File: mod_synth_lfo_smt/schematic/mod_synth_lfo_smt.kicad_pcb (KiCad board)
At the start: 2 copper layers, 39.4 x 109.2 mm, 75 parts, among them J1 CV, J2 Conn_02x08_Odd_Even, J3 SIN, J4 COS, J5 TRI, J6 SQR, J7 RAMP UP, J8 RAMP DOWN, Q1 BC550, Q2 BC550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

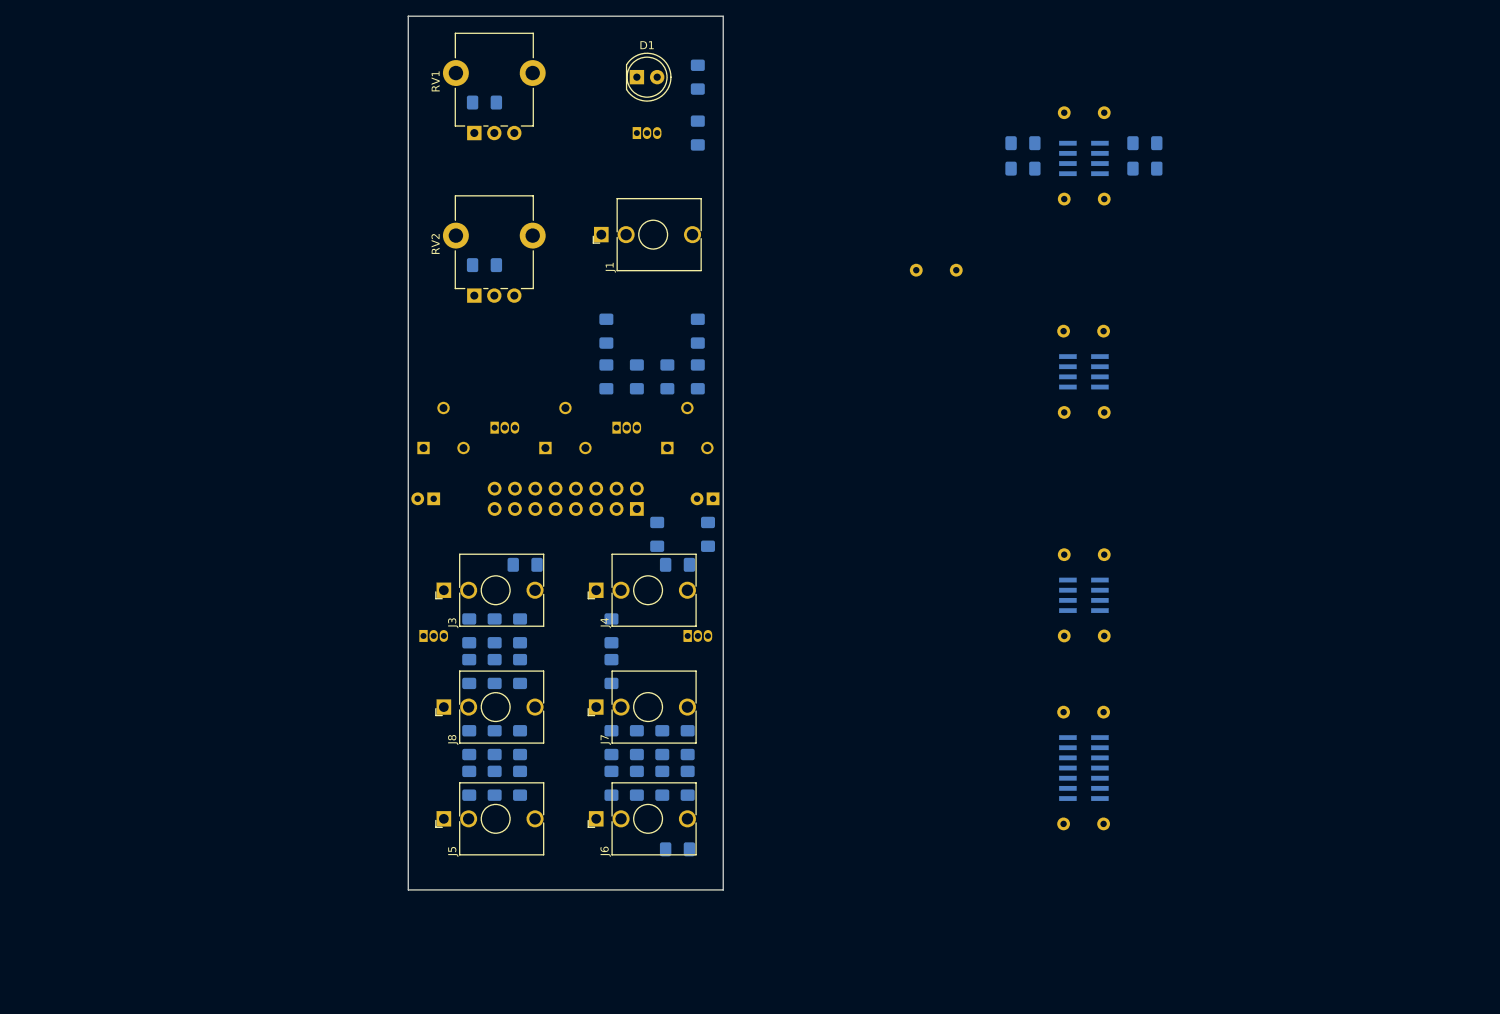
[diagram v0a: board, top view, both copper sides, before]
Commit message: Alter PCB layouts
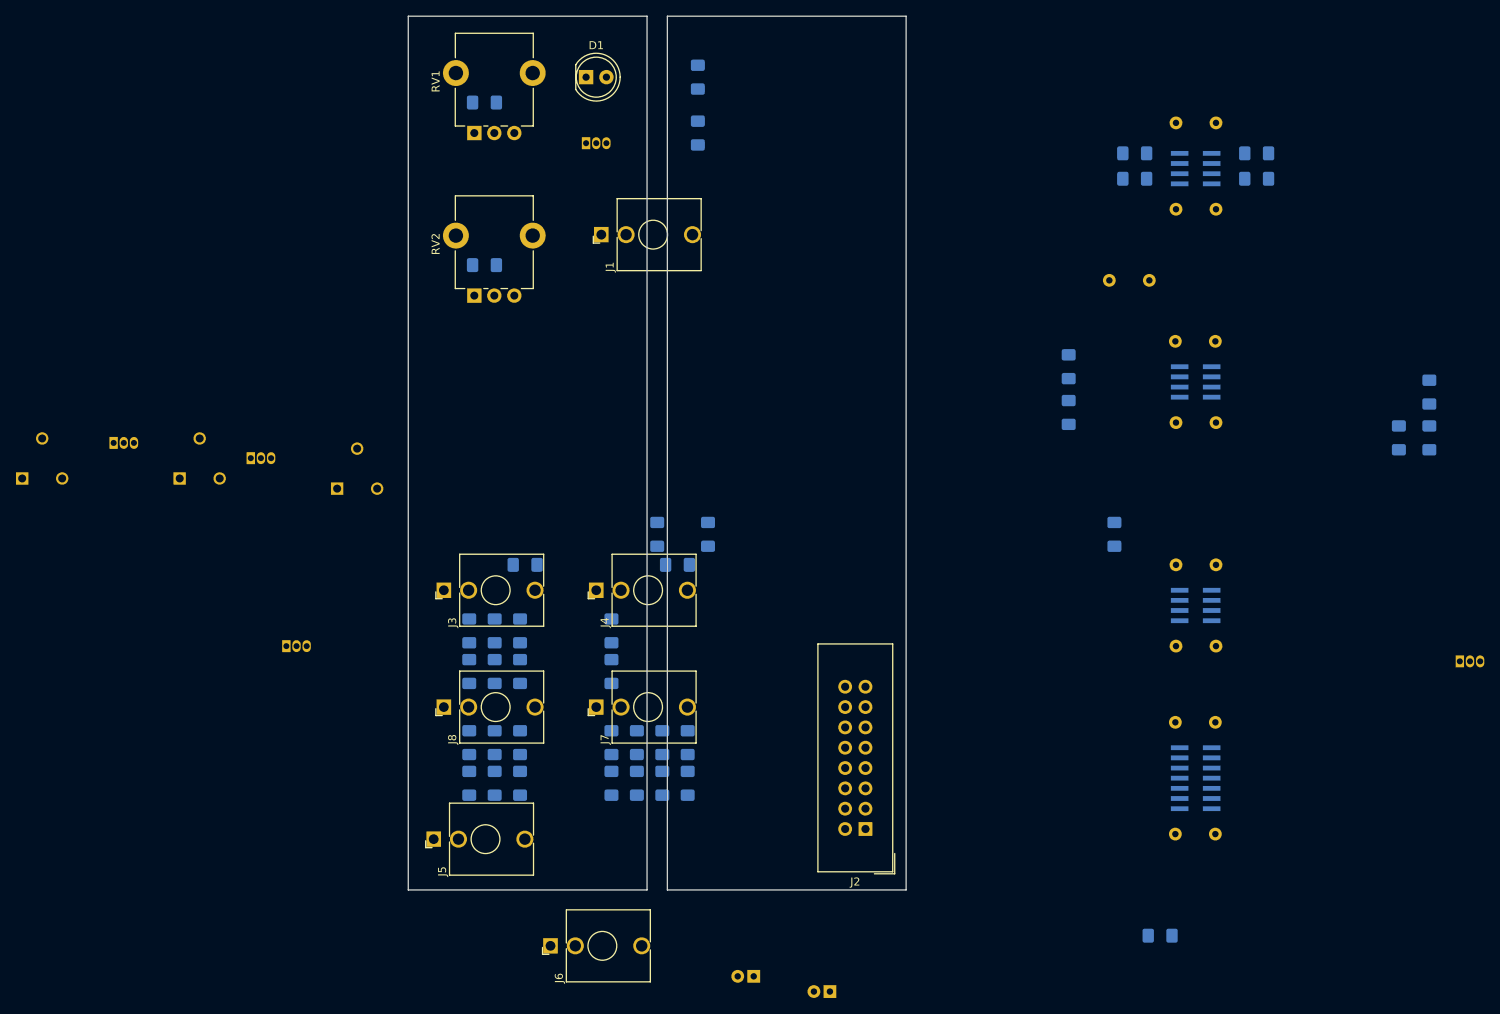
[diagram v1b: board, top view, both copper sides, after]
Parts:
- J2: moved to F.Cu
- moved Q3 96.6 mm to (201.9, 103.5)
- moved R10 91.8 mm to (194.3, 75.6)
- moved R7 91.8 mm to (198.1, 75.6)
- moved R8 91.8 mm to (198.1, 69.8)
- moved C1 71.9 mm to (113.7, 142.9)
- moved C2 63.3 mm to (123.2, 144.8)
- moved R13 62.9 mm to (158.8, 87.6)
- moved R23 61.3 mm to (164.5, 137.8)
- moved R11 58.0 mm to (153.0, 72.4)
- moved R9 58.0 mm to (153.0, 66.7)
- moved RV3 50.3 mm to (22.2, 80.6)
- moved J2 49.2 mm to (127.6, 124.5), turned to 180 degrees
- moved Q2 47.7 mm to (33.7, 76.2)
- moved Q1 45.9 mm to (50.8, 78.1)
- moved RV4 45.9 mm to (41.9, 80.6)
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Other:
- board size 39.4 x 109.2 mm -> 62.2 x 109.2 mm
